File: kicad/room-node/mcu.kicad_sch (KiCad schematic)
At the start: 27 parts, among them J201 USB_C_Receptacle_USB2.0_16P, SW201 SW_Push, SW202 SW_Push, SW203 SW_Push, U201 ESP32-S3-WROOM-1-N16R8, U202 AP1117-33, U203 USBLC6-2SC6

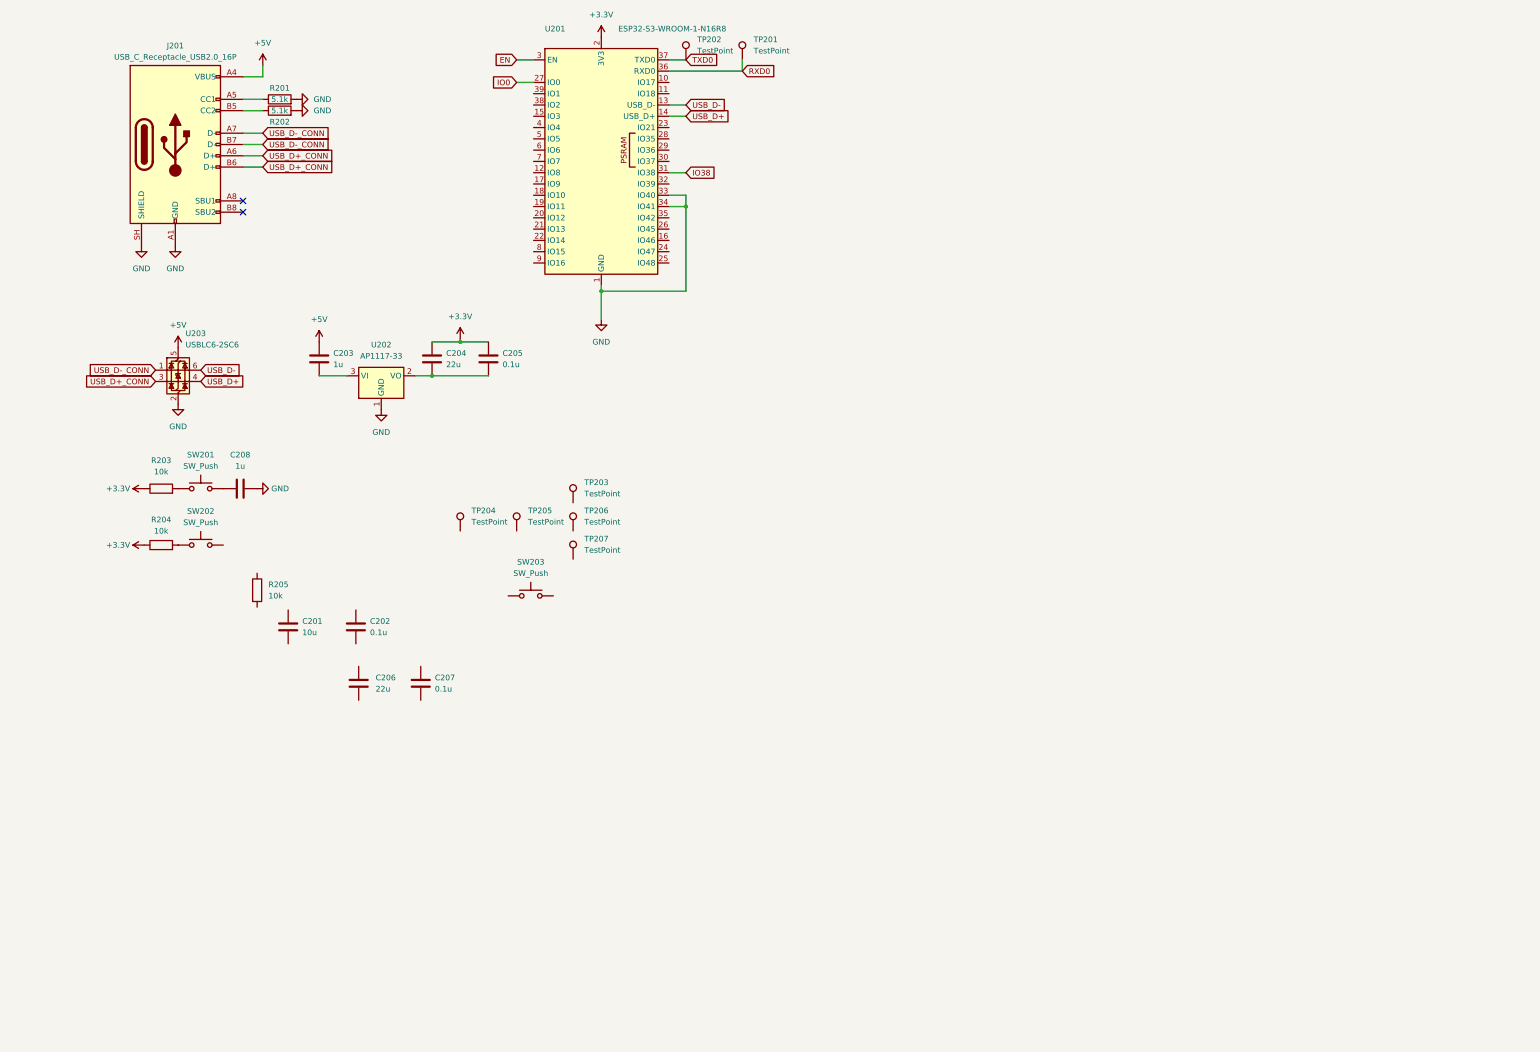
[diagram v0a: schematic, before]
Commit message: SQU-27: Draw rev A schematic (6 sheets + root hierarchy)
- Draw mcu, audio_out, microphone, led_ring, sensors and display sheets
  from docs/pcb/schematic.md: doc refs, values, footprints, MPN and LCSC
  fields. The old MCU sheet (2xx refs, wiring errors) is redrawn.
- Root sheet now holds the 6 sheets as a normal hierarchy; the project
  no longer lists every file as a KiCad 10 top-level sheet, so project
  ERC and netlist cover all sheets.
- Project library: replace the wrong 4-pin AHT20 with a 6-pin symbol and
  6-pad footprint from LCSC C2757850 (pin 1 top-left, datasheet v1.1 s3);
  remove the wrong SPH0645 part (stock part is used); fix the library
  header so KiCad can load it (kicad_symbol_lib, version 20251024).
- tools/check_pinout.py: checks the netlist against pinout.md and the
  other end of each net against schematic.md.
- reports/schematic: ERC report (0 errors, 1 warning), netlist check
  (PASS), PDF of all 7 sheets.
- schematic.md: update status, refs and library notes.

Co-Authored-By: Claude Opus 5.5 <noreply@anthropic.com>
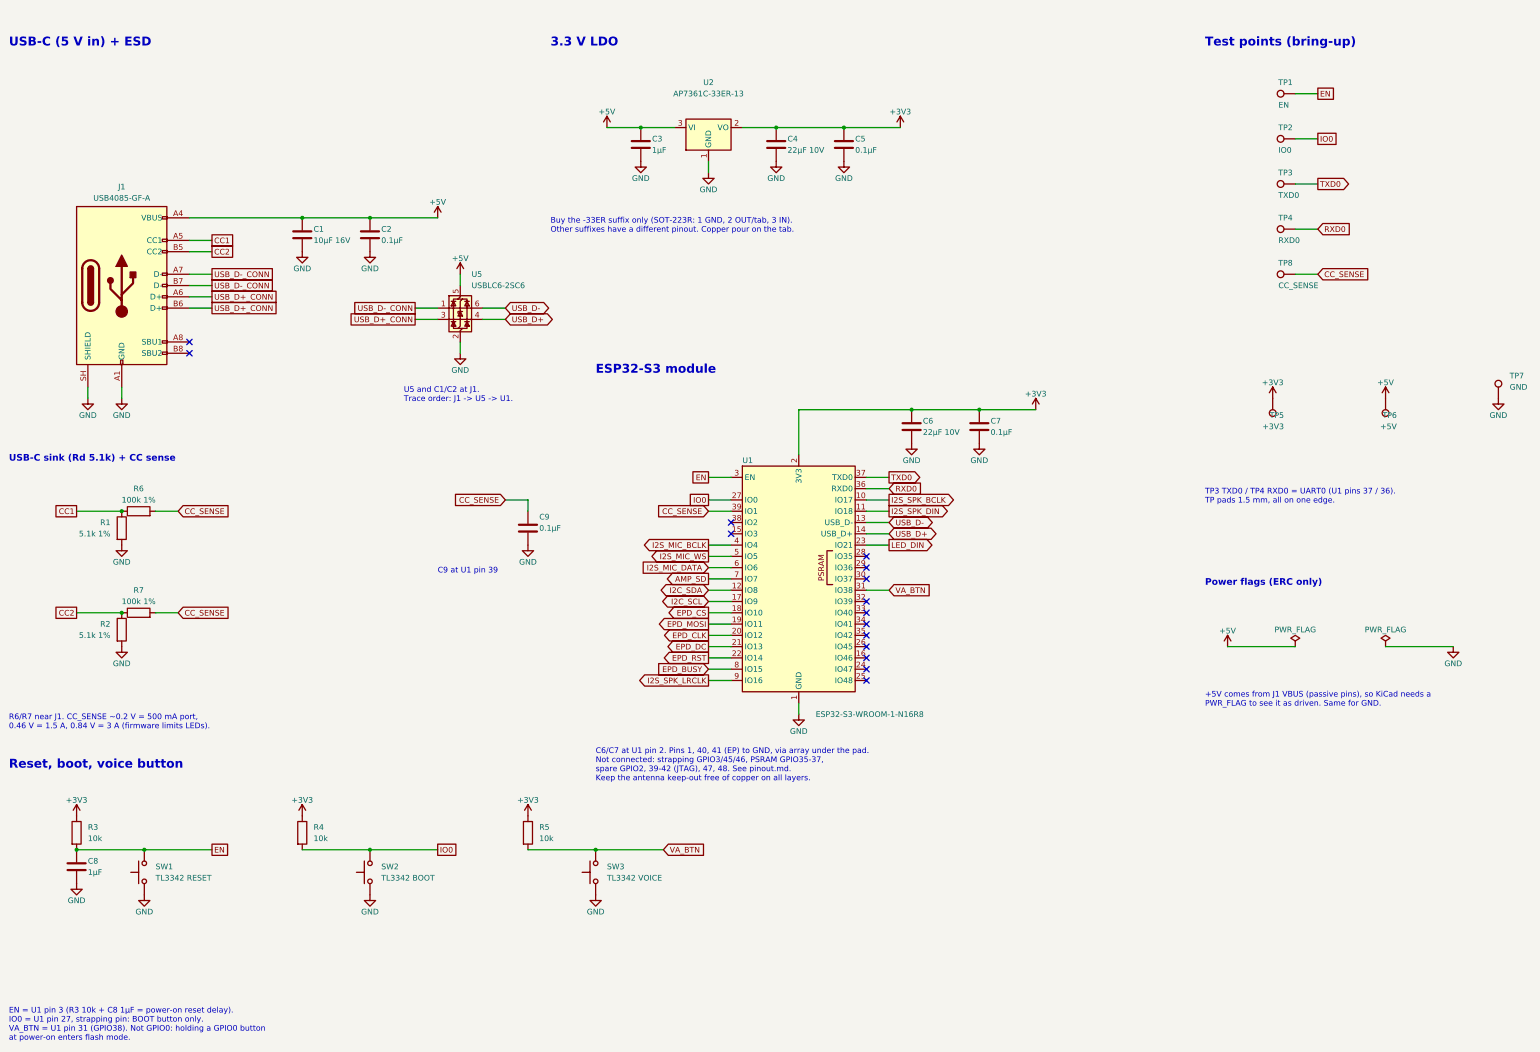
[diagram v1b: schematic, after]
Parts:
- removed C201: 10u, Capacitor_SMD:C_0805_2012Metric, symbol Device:C
- removed C202, C205, C207: 0.1u, Capacitor_SMD:C_0603_1608Metric, symbol Device:C
- removed C203, C208: 1u, Capacitor_SMD:C_0603_1608Metric, symbol Device:C
- removed C204, C206: 22u, Capacitor_SMD:C_0805_2012Metric, symbol Device:C
- removed J201: USB_C_Receptacle_USB2.0_16P, symbol Connector:USB_C_Receptacle_USB2.0_16P
- removed R201, R202: 5.1k, Resistor_SMD:R_0603_1608Metric, symbol Device:R
- removed R203, R204, R205: 10k, Resistor_SMD:R_0603_1608Metric, symbol Device:R
- removed SW201, SW202, SW203: SW_Push, Button_Switch_SMD:SW_SPST_TL3342, symbol Switch:SW_Push
- removed TP201, TP202, TP203, TP204, TP205, TP206, TP207: TestPoint, TestPoint:TestPoint_Pad_D1.5mm, symbol Connector:TestPoint
- removed U201: ESP32-S3-WROOM-1-N16R8, RF_Module:ESP32-S3-WROOM-1, symbol RF_Module:ESP32-S3-WROOM-1
- removed U202: AP1117-33, Package_TO_SOT_SMD:SOT-223-3_TabPin2, symbol Regulator_Linear:AP1117-33
- removed U203: USBLC6-2SC6, Package_TO_SOT_SMD:SOT-23-6, symbol Power_Protection:USBLC6-2SC6
- added C1: 10µF 16V, Capacitor_SMD:C_0805_2012Metric, symbol Device:C
- added C2, C5, C7, C9: 0.1µF, Capacitor_SMD:C_0603_1608Metric, symbol Device:C
- added C3, C8: 1µF, Capacitor_SMD:C_0603_1608Metric, symbol Device:C
- added C4, C6: 22µF 10V, Capacitor_SMD:C_0805_2012Metric, symbol Device:C
- added J1: USB4085-GF-A, Connector_USB:USB_C_Receptacle_GCT_USB4085, symbol Connector:USB_C_Receptacle_USB2.0_16P
- added R1, R2: 5.1k 1%, Resistor_SMD:R_0603_1608Metric, symbol Device:R
- added R3, R4, R5: 10k, Resistor_SMD:R_0603_1608Metric, symbol Device:R
- added R6, R7: 100k 1%, Resistor_SMD:R_0603_1608Metric, symbol Device:R
- added SW1: TL3342 RESET, Button_Switch_SMD:SW_SPST_TL3342, symbol Switch:SW_Push
- added SW2: TL3342 BOOT, Button_Switch_SMD:SW_SPST_TL3342, symbol Switch:SW_Push
- added SW3: TL3342 VOICE, Button_Switch_SMD:SW_SPST_TL3342, symbol Switch:SW_Push
- added TP1: EN, TestPoint:TestPoint_Pad_D1.5mm, symbol Connector:TestPoint
- added TP2: IO0, TestPoint:TestPoint_Pad_D1.5mm, symbol Connector:TestPoint
- added TP3: TXD0, TestPoint:TestPoint_Pad_D1.5mm, symbol Connector:TestPoint
- added TP4: RXD0, TestPoint:TestPoint_Pad_D1.5mm, symbol Connector:TestPoint
- added TP5: +3V3, TestPoint:TestPoint_Pad_D1.5mm, symbol Connector:TestPoint
- added TP6: +5V, TestPoint:TestPoint_Pad_D1.5mm, symbol Connector:TestPoint
- added TP7: GND, TestPoint:TestPoint_Pad_D1.5mm, symbol Connector:TestPoint
- added TP8: CC_SENSE, TestPoint:TestPoint_Pad_D1.5mm, symbol Connector:TestPoint
- added U1: ESP32-S3-WROOM-1-N16R8, RF_Module:ESP32-S3-WROOM-1, symbol RF_Module:ESP32-S3-WROOM-1
- added U2: AP7361C-33ER-13, Package_TO_SOT_SMD:SOT-223-3_TabPin2, symbol Regulator_Linear:AP1117-33
- added U5: USBLC6-2SC6, Package_TO_SOT_SMD:SOT-23-6, symbol Power_Protection:USBLC6-2SC6
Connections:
- net +5V: now also C1.1, C2.1, C3.1, J1.A4 (VBUS), J1.A9 (VBUS), J1.B4 (VBUS), J1.B9 (VBUS), TP6.1, U2.3 (VI), U5.5 (VBUS)
- net EN: now also C8.1, R3.2, SW1.2, TP1.1, U1.3 (EN)
- net GND: now also C1.2, C2.2, C3.2, C4.2, C5.2, C6.2, C7.2, C8.2, C9.2, J1.A1 (GND), J1.A12 (GND), J1.B1 (GND), J1.B12 (GND), J1.SH (SHIELD), R1.2, R2.2, SW1.1, SW2.1, SW3.1, TP7.1, U1.1 (GND), U1.40 (GND), U1.41 (GND), U2.1 (GND), U5.2 (GND)
- net IO0: now also R4.2, SW2.2, TP2.1, U1.27 (IO0)
- net RXD0: now also TP4.1, U1.36 (RXD0)
- net TXD0: now also TP3.1, U1.37 (TXD0)
- net USB_D+: now also U1.14 (USB_D+), U5.4 (I/O2)
- net USB_D+_CONN: now also J1.A6 (D+), J1.B6 (D+), U5.3 (I/O2)
- net USB_D-: now also U1.13 (USB_D-), U5.6 (I/O1)
- net USB_D-_CONN: now also J1.A7 (D-), J1.B7 (D-), U5.1 (I/O1)
- new net +3V3: C4.1, C5.1, C6.1, C7.1, R3.1, R4.1, R5.1, TP5.1, U1.2 (3V3), U2.2 (VO)
- new net AMP_SD: U1.7 (IO7)
- new net CC1: J1.A5 (CC1), R1.1, R6.1
- new net CC2: J1.B5 (CC2), R2.1, R7.1
- new net CC_SENSE: C9.1, R6.2, R7.2, TP8.1, U1.39 (IO1)
- new net EPD_BUSY: U1.8 (IO15)
- new net EPD_CLK: U1.20 (IO12)
- new net EPD_CS: U1.18 (IO10)
- new net EPD_DC: U1.21 (IO13)
- new net EPD_MOSI: U1.19 (IO11)
- new net EPD_RST: U1.22 (IO14)
- new net I2C_SCL: U1.17 (IO9)
- new net I2C_SDA: U1.12 (IO8)
- new net I2S_MIC_BCLK: U1.4 (IO4)
- new net I2S_MIC_DATA: U1.6 (IO6)
- new net I2S_MIC_WS: U1.5 (IO5)
- new net I2S_SPK_BCLK: U1.10 (IO17)
- new net I2S_SPK_DIN: U1.11 (IO18)
- new net I2S_SPK_LRCLK: U1.9 (IO16)
- new net LED_DIN: U1.23 (IO21)
- new net VA_BTN: R5.2, SW3.2, U1.31 (IO38)
- no-connect marks 2 -> 15
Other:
- note added: "+5V comes from J1 VBUS (passive pins), so KiCad needs a PWR_FLAG to see it as driven. Same for GND."
- note added: "3.3 V LDO"
- note added: "Buy the -33ER suffix only (SOT-223R: 1 GND, 2 OUT/tab, 3 IN). Other suffixes have a different pinout. Copper pour on the tab."
- note added: "C6/C7 at U1 pin 2. Pins 1, 40, 41 (EP) to GND, via array under the pad. Not connected: strapping GPIO3/45/46, PSRAM GPIO35-37, spare GPIO2, 39-42 (JTAG), 47, 48. See pinout.md. Keep the antenna keep-out free of copper on all layers."
- note added: "C9 at U1 pin 39"
- note added: "EN = U1 pin 3 (R3 10k + C8 1µF = power-on reset delay). IO0 = U1 pin 27, strapping pin: BOOT button only. VA_BTN = U1 pin 31 (GPIO38). Not GPIO0: holding a GPIO0 button at power-on enters flash mode."
- note added: "ESP32-S3 module"
- note added: "Power flags (ERC only)"
- note added: "R6/R7 near J1. CC_SENSE ~0.2 V = 500 mA port, 0.46 V = 1.5 A, 0.84 V = 3 A (firmware limits LEDs)."
- note added: "Reset, boot, voice button"
- note added: "TP3 TXD0 / TP4 RXD0 = UART0 (U1 pins 37 / 36). TP pads 1.5 mm, all on one edge."
- note added: "Test points (bring-up)"
- note added: "U5 and C1/C2 at J1. Trace order: J1 -> U5 -> U1."
- note added: "USB-C (5 V in) + ESD"
- note added: "USB-C sink (Rd 5.1k) + CC sense"
- company: (none) -> Squarewave Labs
- title: (none) -> Room node rev A - MCU, power, USB

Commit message: SQU-29: Add status LED on GPIO2 (D1 + R12)
- MCU sheet: U1 pin 38 (GPIO2) -> STATUS_LED -> R12 1k -> D1 green LED
  -> GND, active HIGH. Remove the GPIO2 no-connect flag; update the
  U1 note. No change to LED_DIN (no level-shifter pads).
- D1 is KT-0805G (C2297, JLC Basic). JLC Basic has no green or blue
  0603 LED; 0603 alternate is KT-0603G (C12624, Extended).
- pinout.md: GPIO2 is now used; drop the optional test pad note; add
  why GPIO2 is safe (not an S3 strapping pin).
- schematic.md: parts, connections, current (0.5-0.9 mA), polarity
  note (KENTO pad 1 = anode, KiCad pad 1 = cathode).
- BOM: add R12 (C21190) and D1 (C2297) rows.
- check_pinout.py: expect STATUS_LED, R12.2 = D1.2, D1.1 on GND.
- reports: ERC (0 errors, same 1 warning), netlist check PASS, PDF.

Co-Authored-By: Claude Opus 5.5 <noreply@anthropic.com>
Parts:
- added D1: KT-0805G green, LED_SMD:LED_0805_2012Metric, symbol Device:LED
- added R12: 1k, Resistor_SMD:R_0603_1608Metric, symbol Device:R
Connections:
- net GND: now also D1.1 (K)
- net STATUS_LED: now reaches U1.38 (IO2)
- net STATUS_LED: now also R12.1
- new net: D1.2 (A), R12.2
- no-connect marks 15 -> 14
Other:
- note added: "C6/C7 at U1 pin 2. Pins 1, 40, 41 (EP) to GND, via array under the pad. Not connected: strapping GPIO3/45/46, PSRAM GPIO35-37, spare GPIO39-42 (JTAG), 47, 48. GPIO2 = status LED. See pinout.md. Keep the antenna keep-out free of copper on all layers."
- note added: "Status LED (GPIO2)"
- note added: "U1 pin 38 (GPIO2), active HIGH. Not a strapping pin. ~0.5-0.9 mA (Vf 2.4-2.8 V at 1 mA). Firmware can dim it with PWM. Put D1 where it shows through the case."
- note removed: "C6/C7 at U1 pin 2. Pins 1, 40, 41 (EP) to GND, via array under the pad. Not connected: strapping GPIO3/45/46, PSRAM GPIO35-37, spare GPIO2, 39-42 (JTAG), 47, 48. See pinout.md. Keep the antenna keep-out free of copper on all layers."

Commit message: SQU-17: remove voice button SW3 + R5 (wake word only)
Chris: no voice button. U1 pin 31 (GPIO38) gets a no-connect flag.
Schematic, board (parts, 13 tracks/vias, +3V3 stub), BOM, docs,
pinout check and pcb_build.py updated. Gerbers, PDF, pictures regenerated.
ERC: 0 errors, 1 accepted warning. DRC: 0 errors, 0 unconnected,
0 parity issues, 53 silkscreen warnings. Pinout check: PASS.

Co-Authored-By: Claude Opus 5.5 <noreply@anthropic.com>
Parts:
- removed R5: 10k, Resistor_SMD:R_0603_1608Metric, symbol Device:R
- removed SW3: TL3342 VOICE, Button_Switch_SMD:SW_SPST_TL3342, symbol Switch:SW_Push
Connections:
- net VA_BTN: no longer names the net of U1.31 (IO38)
- no-connect marks 14 -> 15
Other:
- note added: "EN = U1 pin 3 (R3 10k + C8 1µF = power-on reset delay). IO0 = U1 pin 27, strapping pin: BOOT button only. U1 pin 31 (GPIO38): not used (no voice button, wake word only)."
- note removed: "EN = U1 pin 3 (R3 10k + C8 1µF = power-on reset delay). IO0 = U1 pin 27, strapping pin: BOOT button only. VA_BTN = U1 pin 31 (GPIO38). Not GPIO0: holding a GPIO0 button at power-on enters flash mode."
